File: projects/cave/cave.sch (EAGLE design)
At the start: 121 parts, among them U1 IRLML6344TRPBF, U10 IRLML6344TRPBF, U11 IRLML6344TRPBF, U12 IRLML6344TRPBF, U2 TLC555CDR, U3 IRLML6344TRPBF, U4 IRLML6344TRPBF, U5 IRLML6344TRPBF, U6 IRLML6344TRPBF, U7 TPS54625, U9 IRLML6344TRPBF

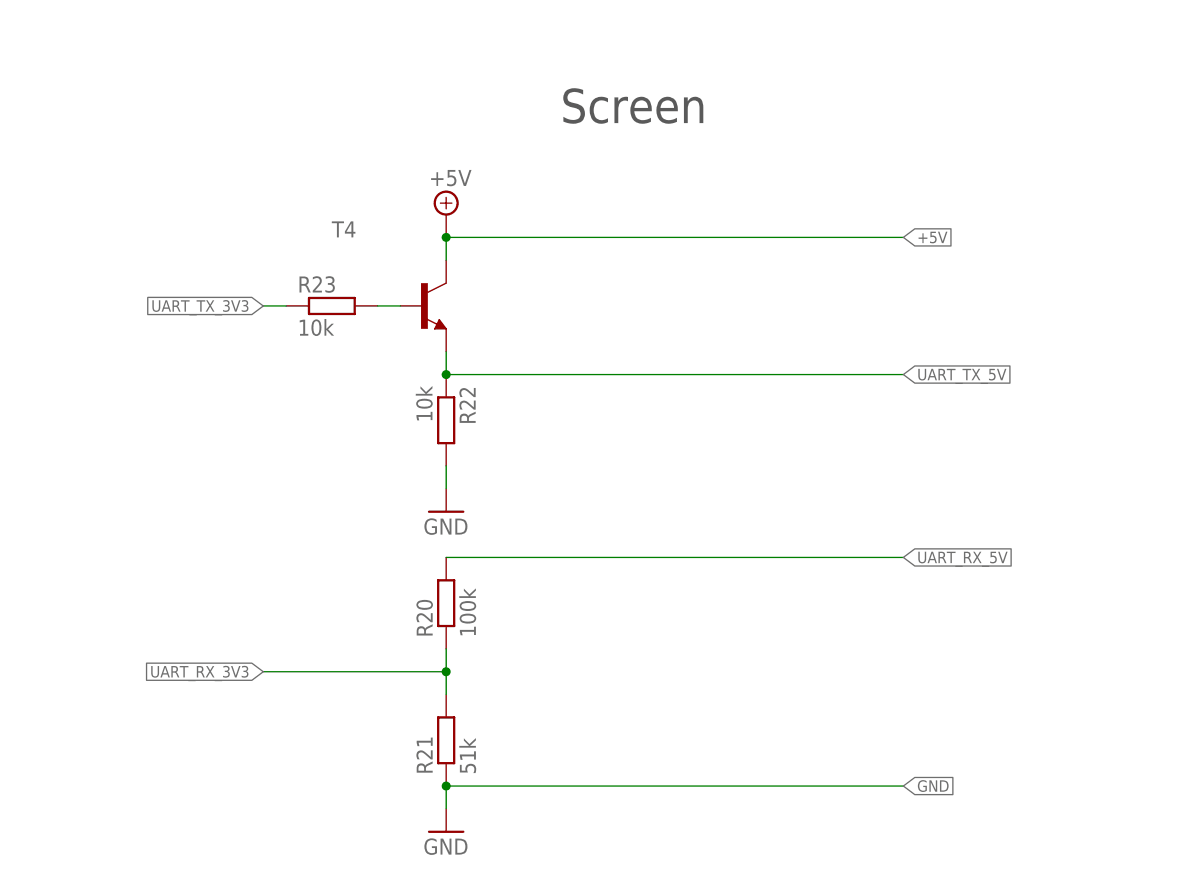
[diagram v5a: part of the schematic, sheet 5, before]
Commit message: UART TX level shifter was NOT working, updated schematic and board.
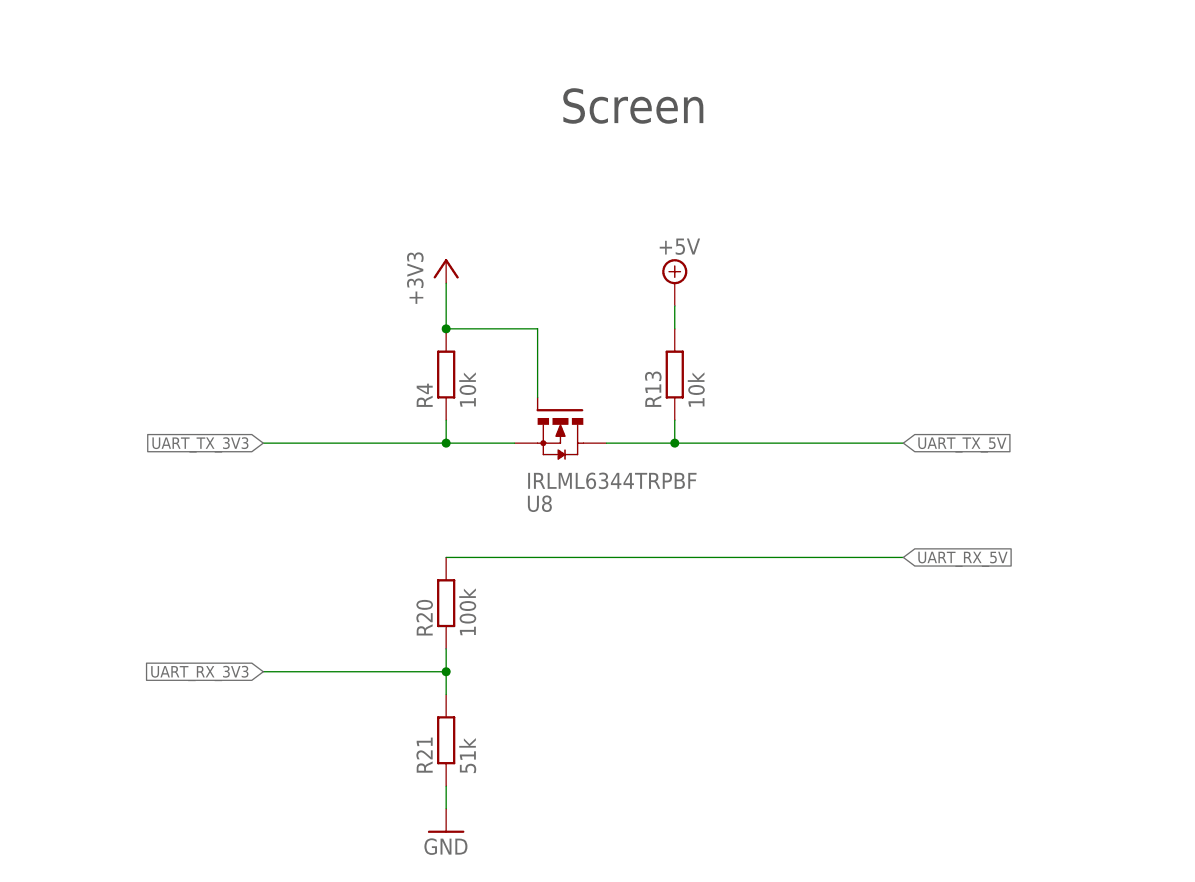
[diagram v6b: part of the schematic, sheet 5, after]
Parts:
- removed R22, R23: 10k, rcl:R-EU_R0603
- removed T4: (no value), transistor:MMBT2369LT1-NPN-SOT23-BEC
- added R13: 10k, rcl:R-EU_R0603
- added U8: IRLML6344TRPBF, transistor-power:IRLML6344TRPBF
- R4: value 100 -> 10k
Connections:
- removed net N$20: R23.2, T4.B
- removed net N$21: C16.1, LIGHTSEN_SIG.P, R12.2, R4.2
- net +3V3: now also R4.2, U8.G
- net +5V: now also R13.2; no longer T4.C
- net GND: no longer R22.2
- net LIGHT_SENSOR: now also C16.1, LIGHTSEN_SIG.P, R12.2; no longer R4.1
- net UART_TX_3V3: now also R4.1, U8.S; no longer R23.1
- net UART_TX_5V: now also R13.1, U8.D; no longer R22.1, T4.E
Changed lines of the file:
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@@
 <part name="R21" library="rcl" deviceset="R-EU_" device="R0603" value="51k"/>
 <part name="GND10" library="supply1" deviceset="GND" device=""/>
-<part name="T4" library="transistor" deviceset="*-NPN-" device="SOT23-BEC" technology="MMBT2369LT1"/>
-<part name="R22" library="rcl" deviceset="R-EU_" device="R0603" value="10k"/>
-<part name="GND11" library="supply1" deviceset="GND" device=""/>
-<part name="R23" library="rcl" deviceset="R-EU_" device="R0603" value="10k"/>
 <part name="HEAT_SWITCH_GND" library="wirepad" deviceset="WIREPAD" device="2,15/1,0" value="WIREPAD2,15/1,0"/>
 <part name="R24" library="rcl" deviceset="R-EU_" device="R0805" value="255"/>
@@
 <part name="+3V3" library="supply1" deviceset="+3V3" device=""/>
 <part name="SUPPLY13" library="supply2" deviceset="+5V" device=""/>
-<part name="SUPPLY14" library="supply2" deviceset="+5V" device=""/>
 <part name="SUPPLY15" library="supply2" deviceset="+12V" device=""/>
 <part name="U7" library="TPS54625" deviceset="TPS54625" device=""/>
@@
 <part name="C14" library="rcl" deviceset="CPOL-EU" device="E5-10.5" value="4.7F/2.5V"/>
 <part name="C15" library="rcl" deviceset="CPOL-EU" device="E5-10.5" value="4.7F/2.5V"/>
-<part name="R4" library="rcl" deviceset="R-EU_" device="R0603" value="100"/>
 <part name="C16" library="rcl" deviceset="C-EU" device="C0603" value="0.1uF/25V"/>
 <part name="R12" library="rcl" deviceset="POTENTIOMETER_" device="PT_SPIN" value="5k"/>
 <part name="+3V4" library="supply1" deviceset="+3V3" device=""/>
+<part name="U8" library="transistor-power" deviceset="IRLML6344TRPBF" device=""/>
+<part name="R4" library="rcl" deviceset="R-EU_" device="R0603" value="10k"/>
+<part name="R13" library="rcl" deviceset="R-EU_" device="R0603" value="10k"/>
+<part name="+3V5" library="supply1" deviceset="+3V3" device=""/>
+<part name="SUPPLY4" library="supply2" deviceset="+5V" device=""/>
 </parts>
 <sheets>
@@
 <instance part="C4" gate="G$1" x="5.08" y="35.56" rot="MR0"/>
 <instance part="GND6" gate="1" x="5.08" y="25.4" rot="MR0"/>
-<instance part="R4" gate="G$1" x="165.1" y="129.54" rot="MR180"/>
 <instance part="C16" gate="G$1" x="175.26" y="124.46" rot="MR0"/>
 <instance part="R12" gate="1" x="182.88" y="124.46" rot="R90"/>
@@
 </segment>
 </net>
-<net name="N$21" class="0">
-<segment>
-<pinref part="R4" gate="G$1" pin="2"/>
+<net name="LIGHT_SENSOR" class="0">
+<segment>
 <wire x1="170.18" y1="129.54" x2="175.26" y2="129.54" width="0.1524" layer="91"/>
 <pinref part="C16" gate="G$1" pin="1"/>
@@
 <wire x1="182.88" y1="129.54" x2="205.74" y2="129.54" width="0.1524" layer="91"/>
 <junction x="182.88" y="129.54"/>
-</segment>
-</net>
-<net name="LIGHT_SENSOR" class="0">
-<segment>
-<pinref part="R4" gate="G$1" pin="1"/>
-<wire x1="160.02" y1="129.54" x2="154.94" y2="129.54" width="0.1524" layer="91"/>
-<label x="154.94" y="129.54" size="1.27" layer="95" rot="R180" xref="yes"/>
+<label x="170.18" y="129.54" size="1.27" layer="95" rot="R180" xref="yes"/>
 </segment>
 </net>
@@
 <instance part="R21" gate="G$1" x="58.42" y="17.78" rot="R90"/>
 <instance part="GND10" gate="1" x="58.42" y="7.62"/>
-<instance part="T4" gate="G$1" x="55.88" y="66.04"/>
-<instance part="R22" gate="G$1" x="58.42" y="53.34" rot="R270"/>
-<instance part="GND11" gate="1" x="58.42" y="43.18"/>
-<instance part="R23" gate="G$1" x="45.72" y="66.04"/>
 <instance part="GND16" gate="1" x="210.82" y="175.26"/>
 <instance part="R36" gate="G$1" x="223.52" y="180.34"/>
@@
 <instance part="GND18" gate="1" x="220.98" y="45.72" rot="MR0"/>
 <instance part="SUPPLY13" gate="+5V" x="35.56" y="182.88"/>
-<instance part="SUPPLY14" gate="+5V" x="58.42" y="76.2"/>
 <instance part="SUPPLY15" gate="+12V" x="205.74" y="101.6"/>
+<instance part="U8" gate="A" x="71.12" y="50.8" rot="MR180"/>
+<instance part="R4" gate="G$1" x="58.42" y="58.42" rot="R90"/>
+<instance part="R13" gate="G$1" x="83.82" y="58.42" rot="R90"/>
+<instance part="+3V5" gate="G$1" x="58.42" y="71.12"/>
+<instance part="SUPPLY4" gate="+5V" x="83.82" y="68.58"/>
 </instances>
 <busses>
@@
 <wire x1="58.42" y1="12.7" x2="58.42" y2="10.16" width="0.1524" layer="91"/>
 <pinref part="GND10" gate="1" pin="GND"/>
-<wire x1="58.42" y1="12.7" x2="109.22" y2="12.7" width="0.1524" layer="91"/>
-<junction x="58.42" y="12.7"/>
-<label x="109.22" y="12.7" size="1.27" layer="95" xref="yes"/>
-</segment>
-<segment>
-<pinref part="R22" gate="G$1" pin="2"/>
-<pinref part="GND11" gate="1" pin="GND"/>
-<wire x1="58.42" y1="45.72" x2="58.42" y2="48.26" width="0.1524" layer="91"/>
 </segment>
 <segment>
@@
 <net name="UART_TX_3V3" class="0">
 <segment>
-<pinref part="R23" gate="G$1" pin="1"/>
-<wire x1="40.64" y1="66.04" x2="38.1" y2="66.04" width="0.1524" layer="91"/>
-<label x="38.1" y="66.04" size="1.27" layer="95" rot="R180" xref="yes"/>
+<pinref part="U8" gate="A" pin="S"/>
+<pinref part="R4" gate="G$1" pin="1"/>
+<wire x1="66.04" y1="50.8" x2="58.42" y2="50.8" width="0.1524" layer="91"/>
+<wire x1="58.42" y1="50.8" x2="58.42" y2="53.34" width="0.1524" layer="91"/>
+<wire x1="58.42" y1="50.8" x2="38.1" y2="50.8" width="0.1524" layer="91"/>
+<junction x="58.42" y="50.8"/>
+<label x="38.1" y="50.8" size="1.27" layer="95" rot="R180" xref="yes"/>
 </segment>
 </net>
@@
 <net name="UART_TX_5V" class="0">
 <segment>
-<pinref part="R22" gate="G$1" pin="1"/>
-<pinref part="T4" gate="G$1" pin="E"/>
-<wire x1="58.42" y1="58.42" x2="58.42" y2="60.96" width="0.1524" layer="91"/>
-<wire x1="109.22" y1="58.42" x2="58.42" y2="58.42" width="0.1524" layer="91"/>
-<junction x="58.42" y="58.42"/>
-<label x="109.22" y="58.42" size="1.27" layer="95" xref="yes"/>
-</segment>
-</net>
-<net name="N$20" class="0">
-<segment>
-<pinref part="R23" gate="G$1" pin="2"/>
-<pinref part="T4" gate="G$1" pin="B"/>
-<wire x1="50.8" y1="66.04" x2="53.34" y2="66.04" width="0.1524" layer="91"/>
+<pinref part="U8" gate="A" pin="D"/>
+<pinref part="R13" gate="G$1" pin="1"/>
+<wire x1="76.2" y1="50.8" x2="83.82" y2="50.8" width="0.1524" layer="91"/>
+<wire x1="83.82" y1="50.8" x2="83.82" y2="53.34" width="0.1524" layer="91"/>
+<wire x1="83.82" y1="50.8" x2="109.22" y2="50.8" width="0.1524" layer="91"/>
+<junction x="83.82" y="50.8"/>
+<label x="109.22" y="50.8" size="1.27" layer="95" xref="yes"/>
 </segment>
 </net>
@@
 </segment>
 <segment>
-<pinref part="T4" gate="G$1" pin="C"/>
-<wire x1="58.42" y1="71.12" x2="58.42" y2="73.66" width="0.1524" layer="91"/>
-<wire x1="58.42" y1="73.66" x2="109.22" y2="73.66" width="0.1524" layer="91"/>
-<pinref part="SUPPLY14" gate="+5V" pin="+5V"/>
-<junction x="58.42" y="73.66"/>
-<label x="109.22" y="73.66" size="1.27" layer="95" xref="yes"/>
+<pinref part="R13" gate="G$1" pin="2"/>
+<wire x1="83.82" y1="63.5" x2="83.82" y2="66.04" width="0.1524" layer="91"/>
+<pinref part="SUPPLY4" gate="+5V" pin="+5V"/>
 </segment>
 </net>
@@
 </segment>
 </net>
+<net name="+3V3" class="0">
+<segment>
+<pinref part="R4" gate="G$1" pin="2"/>
+<pinref part="U8" gate="A" pin="G"/>
+<wire x1="58.42" y1="63.5" x2="68.58" y2="63.5" width="0.1524" layer="91"/>
+<wire x1="68.58" y1="63.5" x2="68.58" y2="55.88" width="0.1524" layer="91"/>
+<pinref part="+3V5" gate="G$1" pin="+3V3"/>
+<wire x1="58.42" y1="63.5" x2="58.42" y2="68.58" width="0.1524" layer="91"/>
+<junction x="58.42" y="63.5"/>
+</segment>
+</net>

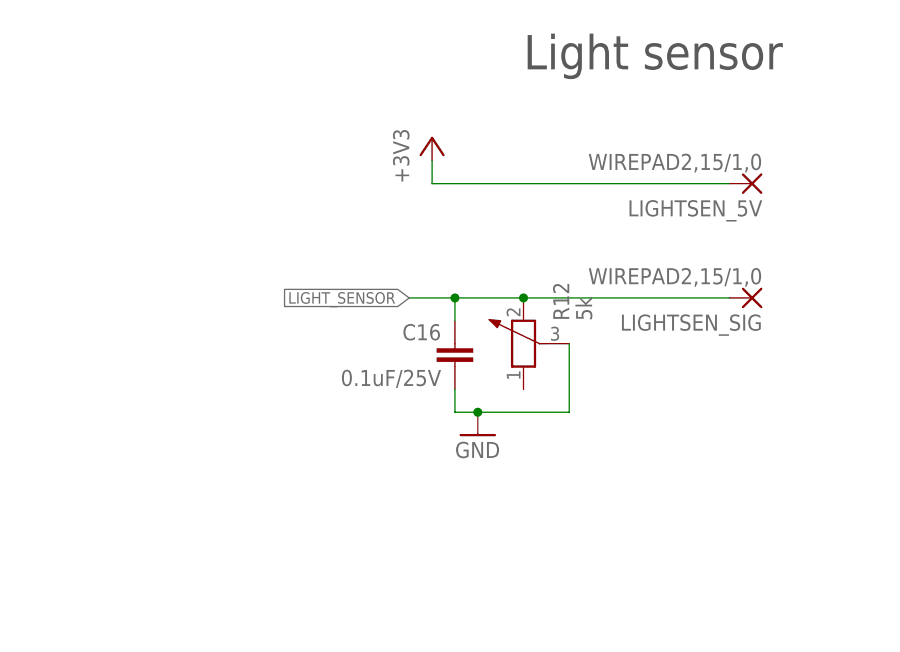
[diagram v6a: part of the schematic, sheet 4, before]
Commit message: Modified light_sensor schematic to improve sensibility, routing to be done (wrong package for potentiometer).
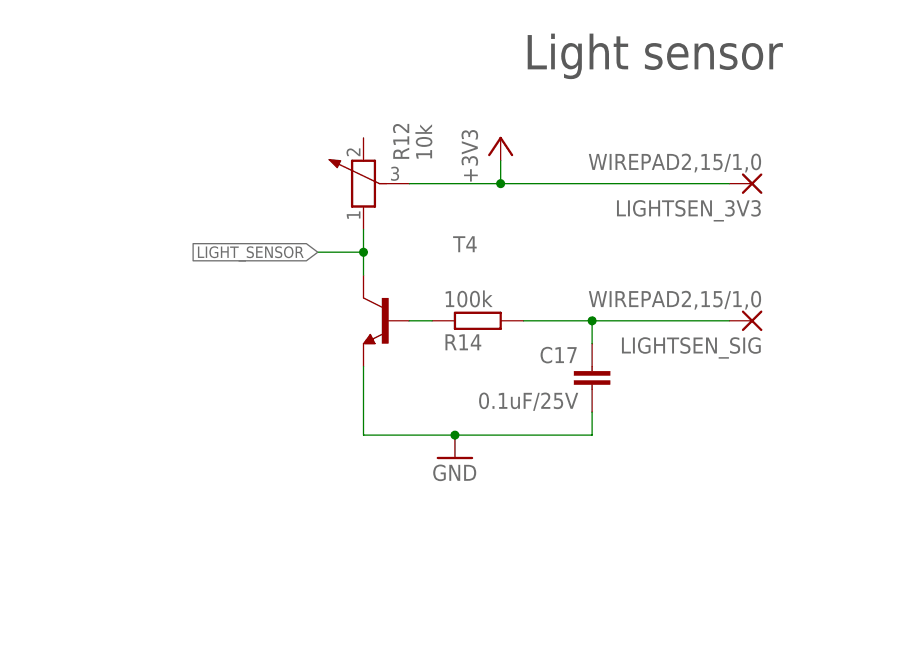
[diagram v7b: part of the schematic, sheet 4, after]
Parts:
- removed C16: 0.1uF/25V, rcl:C-EUC0603
- added C17: 0.1uF/25V, rcl:C-EUC0603
- added R14: 100k, rcl:R-EU_R0603
- added T4: (no value), transistor:MMBT2369LT1-NPN-SOT23-BEC
- R12: value 5k -> 10k
- renumbered LIGHTSEN_5V to LIGHTSEN_3V3
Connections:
- new net N$20: R14.1, T4.B
- new net N$21: C17.1, LIGHTSEN_SIG.P, R14.2
- net +3V3: now also R12.3
- net GND: now also C17.2, T4.E; no longer C16.2, R12.3
- net LIGHT_SENSOR: now also R12.1, T4.C; no longer C16.1, LIGHTSEN_SIG.P, R12.2
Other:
- moved on the sheet: LIGHTSEN_SIG, R12
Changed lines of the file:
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@@
 <part name="R16" library="rcl" deviceset="R-EU_" device="R0603" value="10k"/>
 <part name="GND7" library="supply1" deviceset="GND" device=""/>
-<part name="LIGHTSEN_5V" library="wirepad" deviceset="WIREPAD" device="2,15/1,0" value="WIREPAD2,15/1,0"/>
+<part name="LIGHTSEN_3V3" library="wirepad" deviceset="WIREPAD" device="2,15/1,0" value="WIREPAD2,15/1,0"/>
 <part name="LIGHTSEN_SIG" library="wirepad" deviceset="WIREPAD" device="2,15/1,0" value="WIREPAD2,15/1,0"/>
 <part name="GND8" library="supply1" deviceset="GND" device=""/>
@@
 <part name="C14" library="rcl" deviceset="CPOL-EU" device="E5-10.5" value="4.7F/2.5V"/>
 <part name="C15" library="rcl" deviceset="CPOL-EU" device="E5-10.5" value="4.7F/2.5V"/>
-<part name="C16" library="rcl" deviceset="C-EU" device="C0603" value="0.1uF/25V"/>
-<part name="R12" library="rcl" deviceset="POTENTIOMETER_" device="PT_SPIN" value="5k"/>
+<part name="R12" library="rcl" deviceset="POTENTIOMETER_" device="PT_SPIN" value="10k"/>
 <part name="+3V4" library="supply1" deviceset="+3V3" device=""/>
 <part name="U8" library="transistor-power" deviceset="IRLML6344TRPBF" device=""/>
@@
 <part name="+3V5" library="supply1" deviceset="+3V3" device=""/>
 <part name="SUPPLY4" library="supply2" deviceset="+5V" device=""/>
+<part name="T4" library="transistor" deviceset="*-NPN-" device="SOT23-BEC" technology="MMBT2369LT1"/>
+<part name="R14" library="rcl" deviceset="R-EU_" device="R0603" value="100k"/>
+<part name="C17" library="rcl" deviceset="C-EU" device="C0603" value="0.1uF/25V"/>
 </parts>
 <sheets>
@@
 <instance part="R16" gate="G$1" x="86.36" y="33.02" rot="MR270"/>
 <instance part="GND7" gate="1" x="93.98" y="22.86" rot="MR0"/>
-<instance part="LIGHTSEN_5V" gate="G$1" x="208.28" y="142.24" rot="R180"/>
-<instance part="LIGHTSEN_SIG" gate="G$1" x="208.28" y="129.54" rot="R180"/>
-<instance part="GND8" gate="1" x="177.8" y="114.3"/>
+<instance part="LIGHTSEN_3V3" gate="G$1" x="208.28" y="142.24" rot="R180"/>
+<instance part="LIGHTSEN_SIG" gate="G$1" x="208.28" y="127" rot="R180"/>
+<instance part="GND8" gate="1" x="175.26" y="111.76"/>
 <instance part="+3V1" gate="G$1" x="-15.24" y="147.32"/>
 <instance part="+3V2" gate="G$1" x="78.74" y="147.32"/>
@@
 <instance part="C4" gate="G$1" x="5.08" y="35.56" rot="MR0"/>
 <instance part="GND6" gate="1" x="5.08" y="25.4" rot="MR0"/>
-<instance part="C16" gate="G$1" x="175.26" y="124.46" rot="MR0"/>
-<instance part="R12" gate="1" x="182.88" y="124.46" rot="R90"/>
-<instance part="+3V4" gate="G$1" x="172.72" y="147.32"/>
+<instance part="R12" gate="1" x="165.1" y="142.24" rot="R90"/>
+<instance part="+3V4" gate="G$1" x="180.34" y="147.32"/>
+<instance part="T4" gate="G$1" x="167.64" y="127" rot="MR0"/>
+<instance part="R14" gate="G$1" x="177.8" y="127" rot="MR180"/>
+<instance part="C17" gate="G$1" x="190.5" y="121.92" rot="MR0"/>
 </instances>
 <busses>
@@
 </segment>
 <segment>
-<pinref part="C16" gate="G$1" pin="2"/>
+<pinref part="T4" gate="G$1" pin="E"/>
 <pinref part="GND8" gate="1" pin="GND"/>
-<wire x1="175.26" y1="119.38" x2="175.26" y2="116.84" width="0.1524" layer="91"/>
-<wire x1="175.26" y1="116.84" x2="177.8" y2="116.84" width="0.1524" layer="91"/>
-<pinref part="R12" gate="1" pin="3"/>
-<wire x1="177.8" y1="116.84" x2="187.96" y2="116.84" width="0.1524" layer="91"/>
-<wire x1="187.96" y1="116.84" x2="187.96" y2="124.46" width="0.1524" layer="91"/>
-<junction x="177.8" y="116.84"/>
+<wire x1="165.1" y1="121.92" x2="165.1" y2="114.3" width="0.1524" layer="91"/>
+<wire x1="165.1" y1="114.3" x2="175.26" y2="114.3" width="0.1524" layer="91"/>
+<pinref part="C17" gate="G$1" pin="2"/>
+<wire x1="175.26" y1="114.3" x2="190.5" y2="114.3" width="0.1524" layer="91"/>
+<wire x1="190.5" y1="114.3" x2="190.5" y2="116.84" width="0.1524" layer="91"/>
+<junction x="175.26" y="114.3"/>
 </segment>
 </net>
@@
 </segment>
 <segment>
-<pinref part="LIGHTSEN_5V" gate="G$1" pin="P"/>
-<wire x1="205.74" y1="142.24" x2="172.72" y2="142.24" width="0.1524" layer="91"/>
-<wire x1="172.72" y1="142.24" x2="172.72" y2="144.78" width="0.1524" layer="91"/>
+<pinref part="R12" gate="1" pin="3"/>
 <pinref part="+3V4" gate="G$1" pin="+3V3"/>
+<wire x1="170.18" y1="142.24" x2="180.34" y2="142.24" width="0.1524" layer="91"/>
+<wire x1="180.34" y1="142.24" x2="180.34" y2="144.78" width="0.1524" layer="91"/>
+<pinref part="LIGHTSEN_3V3" gate="G$1" pin="P"/>
+<wire x1="180.34" y1="142.24" x2="205.74" y2="142.24" width="0.1524" layer="91"/>
+<junction x="180.34" y="142.24"/>
 </segment>
 </net>
@@
 </segment>
 </net>
+<net name="N$20" class="0">
+<segment>
+<pinref part="T4" gate="G$1" pin="B"/>
+<pinref part="R14" gate="G$1" pin="1"/>
+<wire x1="170.18" y1="127" x2="172.72" y2="127" width="0.1524" layer="91"/>
+</segment>
+</net>
+<net name="N$21" class="0">
+<segment>
+<pinref part="R14" gate="G$1" pin="2"/>
+<pinref part="C17" gate="G$1" pin="1"/>
+<wire x1="182.88" y1="127" x2="190.5" y2="127" width="0.1524" layer="91"/>
+<wire x1="190.5" y1="127" x2="190.5" y2="124.46" width="0.1524" layer="91"/>
+<pinref part="LIGHTSEN_SIG" gate="G$1" pin="P"/>
+<wire x1="190.5" y1="127" x2="205.74" y2="127" width="0.1524" layer="91"/>
+<junction x="190.5" y="127"/>
+</segment>
+</net>
 <net name="LIGHT_SENSOR" class="0">
 <segment>
-<wire x1="170.18" y1="129.54" x2="175.26" y2="129.54" width="0.1524" layer="91"/>
-<pinref part="C16" gate="G$1" pin="1"/>
-<wire x1="175.26" y1="129.54" x2="182.88" y2="129.54" width="0.1524" layer="91"/>
-<wire x1="175.26" y1="127" x2="175.26" y2="129.54" width="0.1524" layer="91"/>
-<junction x="175.26" y="129.54"/>
-<pinref part="R12" gate="1" pin="2"/>
-<pinref part="LIGHTSEN_SIG" gate="G$1" pin="P"/>
-<wire x1="182.88" y1="129.54" x2="205.74" y2="129.54" width="0.1524" layer="91"/>
-<junction x="182.88" y="129.54"/>
-<label x="170.18" y="129.54" size="1.27" layer="95" rot="R180" xref="yes"/>
-</segment>
-</net>
+<pinref part="T4" gate="G$1" pin="C"/>
+<pinref part="R12" gate="1" pin="1"/>
+<wire x1="165.1" y1="137.16" x2="165.1" y2="134.62" width="0.1524" layer="91"/>
+<wire x1="165.1" y1="134.62" x2="165.1" y2="132.08" width="0.1524" layer="91"/>
+<wire x1="165.1" y1="134.62" x2="160.02" y2="134.62" width="0.1524" layer="91"/>
+<junction x="165.1" y="134.62"/>
+<label x="160.02" y="134.62" size="1.27" layer="95" rot="R180" xref="yes"/>
+</segment>
+</net>
